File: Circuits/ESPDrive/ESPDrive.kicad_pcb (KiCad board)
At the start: 4 copper layers, 44 x 64 mm, 55 parts, among them Q1 AOSS32334C, U1 AP63203WU, U2 AP63201WU, U3 LTV-827S

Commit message: ESPDrive: Final tweaks before manufacture
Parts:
- moved C5 23.0 mm to (145.0, 86.0), turned to 0 degrees
- moved R6 23.0 mm to (145.0, 89.0), turned to 0 degrees
- moved R7 23.0 mm to (145.0, 83.0), turned to 180 degrees
- moved C8 14.1 mm to (147.0, 119.0)
- moved R5 14.0 mm to (154.5, 83.0)
- moved R9 14.0 mm to (145.0, 115.0)
- moved R2 14.0 mm to (158.0, 84.0)
- moved R8 13.5 mm to (144.0, 119.0)
- moved D1 1.00 mm to (155.0, 131.0)
- moved Q1 1.00 mm to (151.0, 131.0)
- moved R3 1.00 mm to (155.0, 128.0)
- moved R4 1.00 mm to (151.0, 128.0)
- moved W4 0.63 mm to (138.9, 134.2)
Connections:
- MCU1 pad 20: C_vdiv -> unconnected-(MCU1-D4-Pad20)
- MCU1 pad 22: C_en -> unconnected-(MCU1-TX2-Pad22)
- MCU1 pad 30: unconnected-(MCU1-D23-Pad30) -> C_en
- MCU1 pad 4: unconnected-(MCU1-D34-Pad4) -> C_vdiv
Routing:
- net +BATT: track 29.4 -> 2.59 mm, vias 21 -> 56
- net +3V3: track 85.4 -> 73.9 mm
- net Net-(U2-EN): track 41.6 -> 52.0 mm
- net +12V: track 0.00 -> 10.1 mm, vias 0 -> 23
- net GNDREF: track 8.86 -> 0.00 mm, vias 0 -> 175
- net C_en: track 5.50 -> 9.65 mm
- net Net-(U1-SW): track 0.00 -> 3.67 mm
- net Net-(U2-SW): track 0.00 -> 3.55 mm
- net D_relay: track 9.00 -> 10.7 mm
- net Net-(U2-FB): track 18.7 -> 17.4 mm, vias 2 -> 1
- net C_relay: track 37.3 -> 38.3 mm
- net C_vdiv: track 11.4 -> 10.9 mm
- added copper zone on B.Cu, net +BATT
- added copper zone on In1.Cu, net +BATT
- added copper zone on In2.Cu, net GNDREF
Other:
- board text added: "2026.05.03"
- board text added: "ESPDrive v1.0"

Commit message: ESPDrive: Added p channel mosfet to voltage divider; versioned to v1.1
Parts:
- removed Q1: AOSS32334C, Package_TO_SOT_SMD:SOT-23-3
- added Q2: AO3401A, Package_TO_SOT_SMD:SOT-23, B.Cu at (149.9, 90.0)
- added Q3: AO3400A, Package_TO_SOT_SMD:SOT-23, B.Cu at (151.0, 131.2)
- added R17: 4.7kΩ, Resistor_SMD:R_0805_2012Metric_Pad1.20x1.40mm_HandSolder, B.Cu at (150.0, 96.0)
- added R18: 22kΩ, Resistor_SMD:R_0805_2012Metric_Pad1.20x1.40mm_HandSolder, B.Cu at (150.0, 93.0)
- L1, L2: footprint Inductor_SMD:L_TechFuse_SL0630 -> Inductor_SMD:L_Abracon_ASPI-0630LR
- R10, R11: value 2.7kΩ -> 2.2kΩ
- R14: value 330Ω -> 68Ω
- R15: value 330Ω -> 10Ω
- R16: value 220Ω -> 10Ω
- moved C13 14.6 mm to (144.1, 94.6), turned to 90 degrees
- moved R12 5.83 mm to (160.0, 104.0), turned to 90 degrees
- moved C14 1.42 mm to (159.1, 92.1), turned to 90 degrees
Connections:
- net C_vdiv renamed Vdiv
- MCU1 pad 11: unconnected-(MCU1-D14-Pad11) -> C_div
- MCU1 pad 13: unconnected-(MCU1-D13-Pad13) -> C_relay
- MCU1 pad 23: C_relay -> unconnected-(MCU1-D5-Pad23)
- MCU1 pad 25: C_on -> unconnected-(MCU1-D19-Pad25)
- MCU1 pad 8: unconnected-(MCU1-D25-Pad8) -> C_on
- R6 pad 2: +BATT -> Net-(Q2-S)
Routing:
- net C_div: track 0.00 -> 15.7 mm, vias 0 -> 1
- net +3V3: track 73.9 -> 62.7 mm
- net C_on: track 24.3 -> 34.0 mm
- net Net-(R10-Pad2): track 34.6 -> 42.6 mm
- net Net-(R11-Pad2): track 43.3 -> 50.7 mm
- net Net-(Q2-G): track 0.00 -> 5.93 mm
- net C_relay: track 38.3 -> 33.6 mm
- net +BATT: track 2.59 -> 6.69 mm, vias 56 -> 68
- net Net-(Q2-S): track 0.00 -> 3.00 mm
- net Net-(D2-RA): track 7.29 -> 8.19 mm
- net GNDREF: vias 175 -> 185
- net +12V: vias 23 -> 31
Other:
- board text added: "Vout"

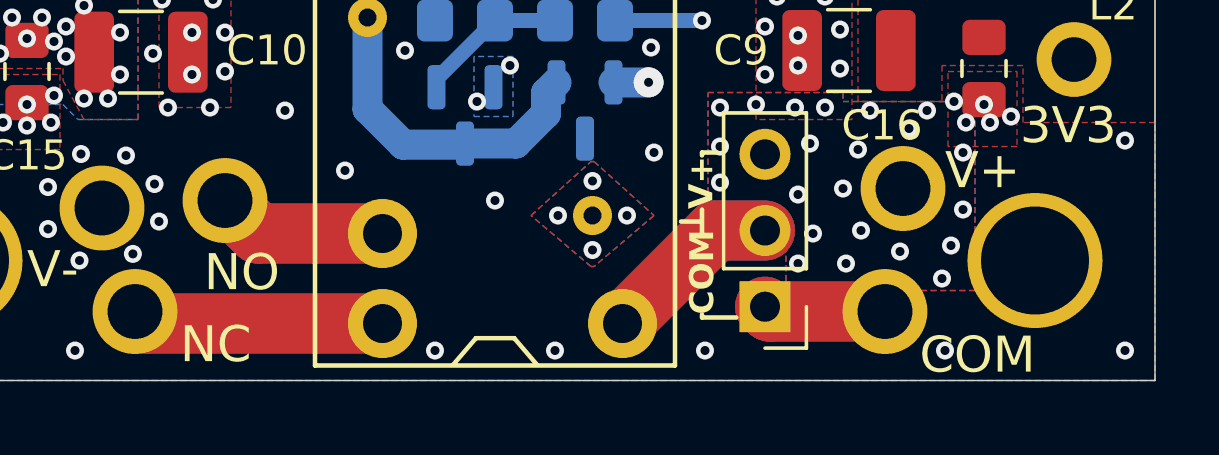
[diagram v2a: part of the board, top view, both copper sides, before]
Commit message: ESPDrive: small tweaks to silkscreens
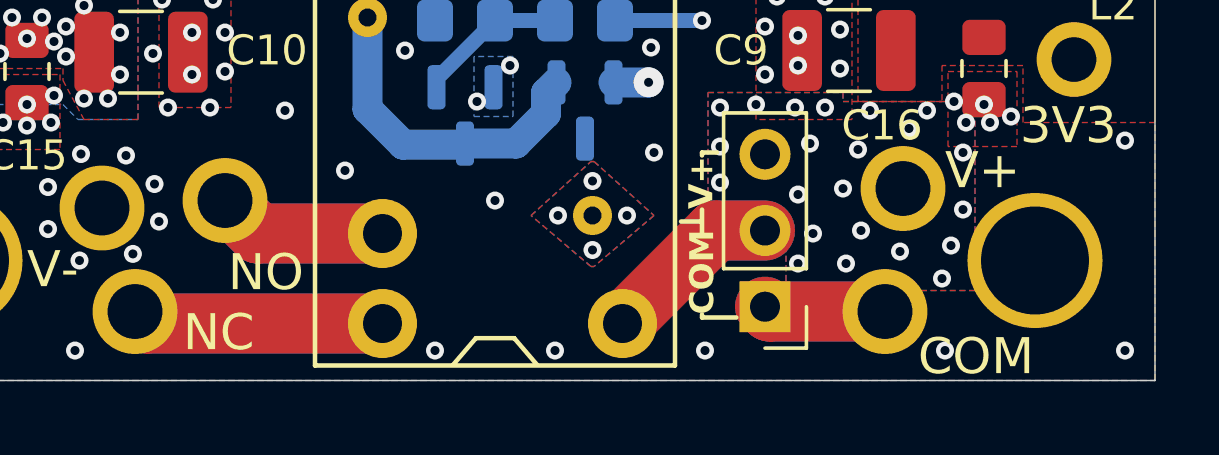
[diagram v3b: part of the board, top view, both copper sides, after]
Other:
- board text added: "2026.05.12"
- board text added: "ESPDrive v1.1"
- board text removed: "12V/5V"
- board text removed: "2026.05.03"
- board text removed: "ESPDrive v1.0"
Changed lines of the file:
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@@
 		)
 		(embedded_fonts no)
-		(model "../../Parts/3D/ESP32-DEVKIT-V1.step"
+		(model "C:/Projects/ehryk.github.com/Circuits/Parts/3D/ESP32-DEVKIT-V1.step"
 			(offset
 				(xyz -1 0 6)
@@
 		)
 		(property "Value" "6.8μH"
-			(at 0 4.25 270)
+			(at 0 4.25 90)
 			(layer "F.Fab")
 			(effects
@@
 		)
 		(fp_text user "${REFERENCE}"
-			(at 0 0 270)
+			(at 0 0 90)
 			(layer "F.Fab")
 			(effects
@@
 		)
 		(embedded_fonts no)
-		(model "${KICAD10_3DMODEL_DIR}/Inductor_SMD.3dshapes/L_Abracon_ASPI-0630LR.step"
+		(model "${KICAD10_3DMODEL_DIR}/Inductor_SMD.3dshapes/L_Panasonic_PCC-M0630M.step"
 			(offset
 				(xyz 0 0 0)
@@
 		)
 		(property "Value" "6.8μH"
-			(at 0 4.25 270)
+			(at 0 4.25 90)
 			(layer "F.Fab")
 			(effects
@@
 		)
 		(fp_text user "${REFERENCE}"
-			(at 0 0 270)
+			(at 0 0 90)
 			(layer "F.Fab")
 			(effects
@@
 		)
 		(embedded_fonts no)
-		(model "${KICAD10_3DMODEL_DIR}/Inductor_SMD.3dshapes/L_Abracon_ASPI-0630LR.step"
+		(model "${KICAD10_3DMODEL_DIR}/Inductor_SMD.3dshapes/L_Panasonic_PCC-M0630M.step"
 			(offset
 				(xyz 0 0 0)
@@
 		(tags "resistor handsolder")
 		(property "Reference" "R18"
-			(at 3.5 0 180)
+			(at 3.4 0 180)
 			(layer "B.SilkS")
 			(effects
@@
 		(tags "SOT TO_SOT_SMD")
 		(property "Reference" "D1"
-			(at 1.5 -1.4 180)
+			(at 1.5 -1.8 180)
 			(layer "B.SilkS")
 			(effects
@@
 		(tags "SOT TO_SOT_SMD")
 		(property "Reference" "Q3"
-			(at 0 2.4 90)
+			(at 0 2.6 180)
 			(layer "B.SilkS")
 			(effects
@@
 		(tags "resistor handsolder")
 		(property "Reference" "R14"
-			(at -2.6 0 180)
+			(at -3.5 0.2 180)
 			(layer "B.SilkS")
 			(effects
@@
 		(tags "resistor handsolder")
 		(property "Reference" "R16"
-			(at -2.7 0 180)
+			(at -3.5 0 180)
 			(layer "B.SilkS")
 			(effects
@@
 		(tags "resistor handsolder")
 		(property "Reference" "R6"
-			(at 1.5 1.8 0)
+			(at 1.6 1.7 0)
 			(layer "B.SilkS")
 			(effects
@@
 		(tags "resistor handsolder")
 		(property "Reference" "R15"
-			(at 0 -2.4 180)
+			(at 0.8 -2.4 180)
 			(layer "B.SilkS")
 			(effects
@@
 	)
 	(gr_text "NC"
-		(at 141.5 139.5 0)
+		(at 141.6 139.1 0)
 		(layer "F.SilkS")
 		(effects
@@
 	)
 	(gr_text "NO"
-		(at 142.3 137.1 0)
+		(at 143.1 137.1 0)
 		(layer "F.SilkS")
 		(effects
@@
 	)
 	(gr_text "COM"
-		(at 166.15 139.85 0)
+		(at 166.1 139.9 0)
 		(layer "F.SilkS")
 		(effects
@@
 		)
 	)
-	(gr_text "12V/5V"
-		(at 130 132.6 -0)
+	(gr_text "Vout"
+		(at 130.8 132.1 0)
 		(layer "B.SilkS")
 		(effects
@@
 	)
 	(gr_text "NC"
-		(at 141.5 139.6 -0)
+		(at 141.4 139.1 -0)
 		(layer "B.SilkS")
 		(effects
@@
 	)
 	(gr_text "NO"
-		(at 142.35 137.1 -0)
+		(at 143.3 136.8 -0)
 		(layer "B.SilkS")
 		(effects
@@
 	)
 	(gr_text "V+"
-		(at 162.4 132.2 -0)
+		(at 162.5 132.3 -0)
 		(layer "B.SilkS")
 		(effects
@@
 	)
 	(gr_text "COM"
-		(at 166.2 139.85 -0)
+		(at 167 139.9 -0)
 		(layer "B.SilkS")
 		(effects
@@
 		)
 	)
-	(gr_text "2026.05.03"
+	(gr_text "2026.05.12"
 		(at 152 106 0)
 		(layer "B.SilkS")
@@
 		)
 	)
-	(gr_text "ESPDrive v1.0"
+	(gr_text "ESPDrive v1.1"
 		(at 152 102 0)
 		(layer "B.SilkS")

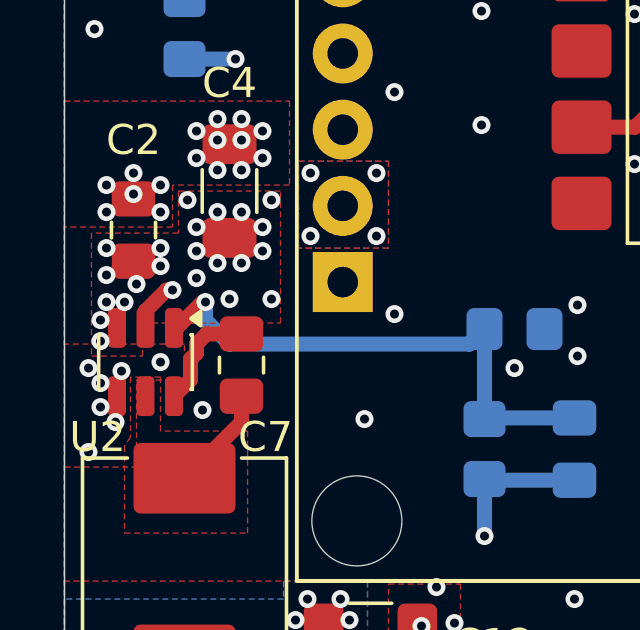
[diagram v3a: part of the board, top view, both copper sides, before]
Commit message: ESPDrive: Added teardrops
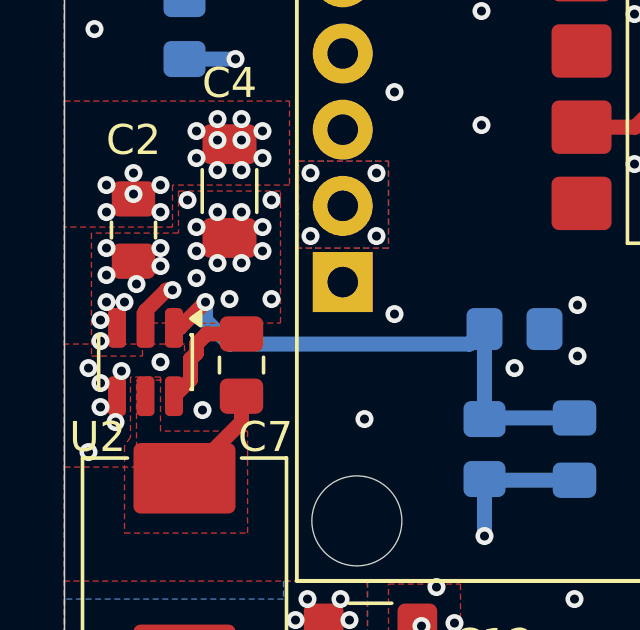
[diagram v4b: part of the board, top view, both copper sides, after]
